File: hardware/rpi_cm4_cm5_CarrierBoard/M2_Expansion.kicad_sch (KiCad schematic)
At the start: 20 parts, among them J23 MDT420M03001, U38 ASAK-32.768KHZ-LRS-T

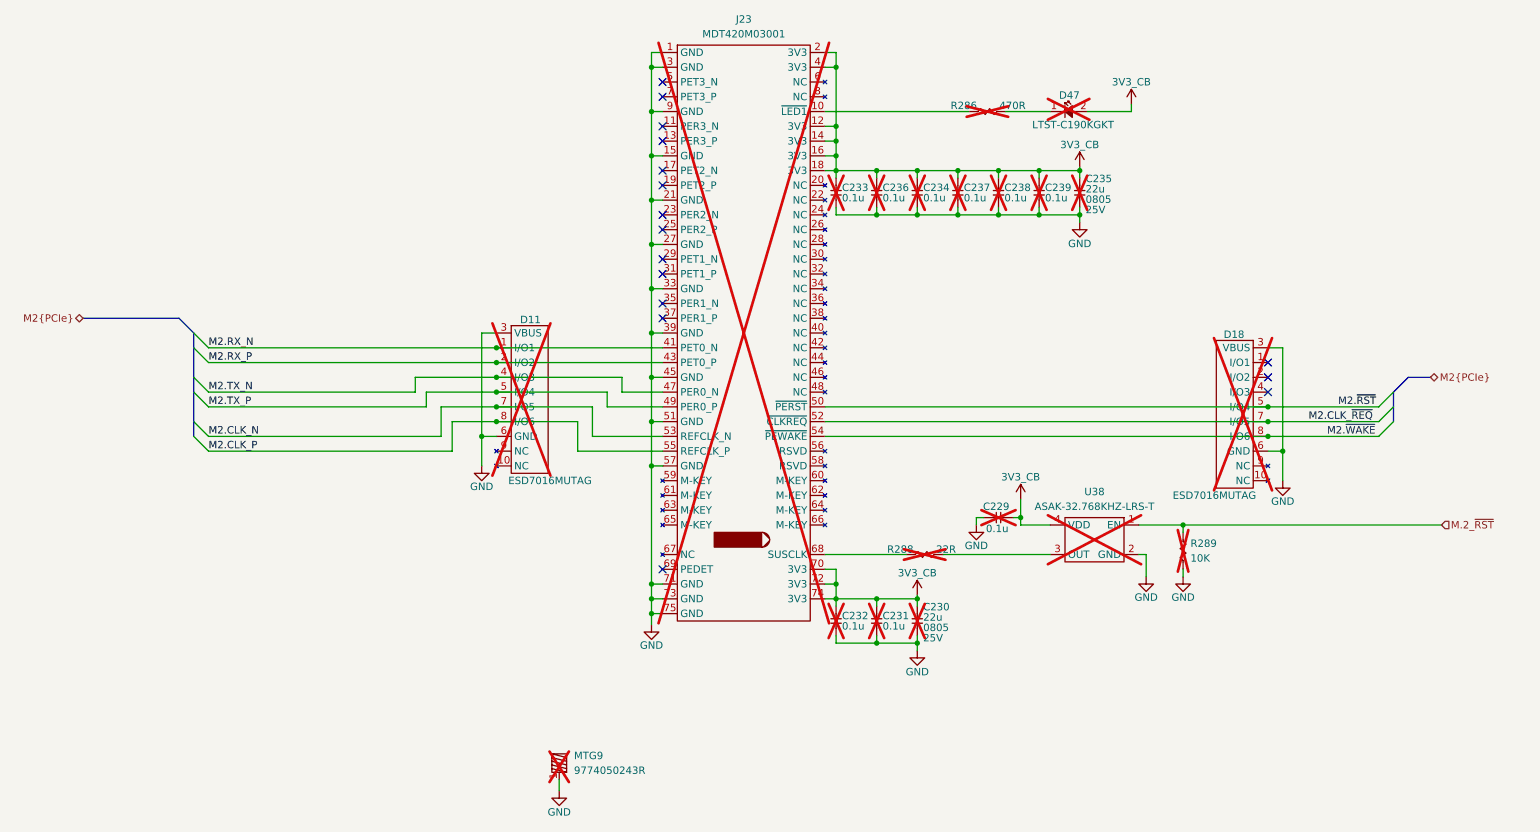
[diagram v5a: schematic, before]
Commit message: Document stackup Few changes to schematic based on preliminary PCB placement Update PinMux based on preliminary PCB placement and component positions
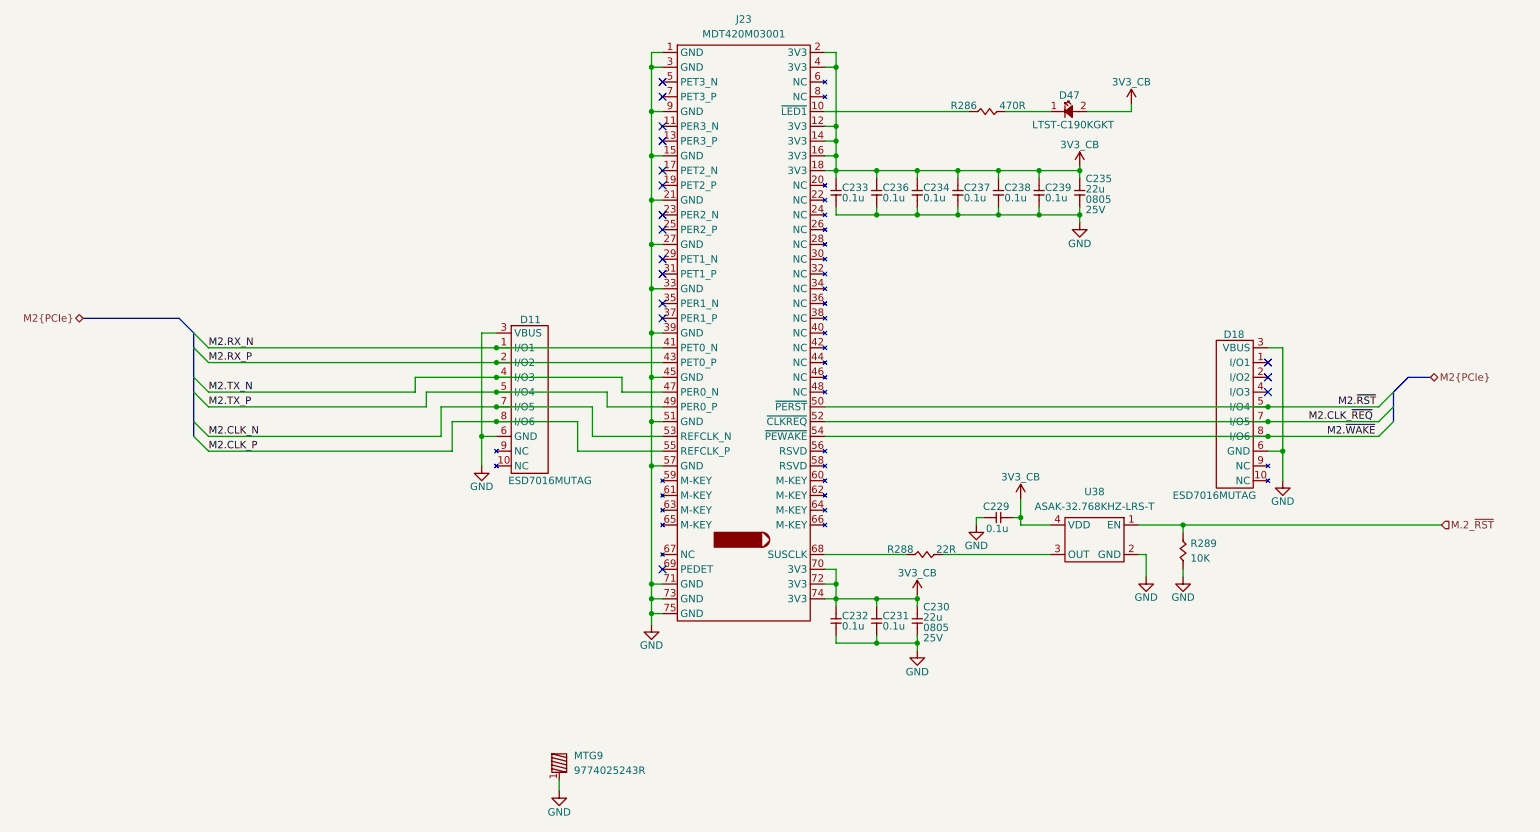
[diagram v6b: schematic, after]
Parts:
- removed MTG9: 9774050243R, footprint:9774050243R, symbol KicadCompDb:Miscellaneous/MISC_00008
- added MTG9: 9774025243R, footprint:9774025243R, symbol KicadCompDb:Miscellaneous/MISC_00009
- C229, C230, C231, C232, C233, C234, C235, C236, C237, C238, C239, D11, D18, D47, J23, R286, R288, R289, U38: now fitted
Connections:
- net GND: now also MTG9.1
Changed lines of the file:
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@@
 	(title_block
 		(title "RPI CMx Carrier")
-		(date "2025-12-07")
+		(date "2026-01-22")
 		(rev "2.00-0A")
 		(comment 1 "Jean-Francois Bilodeau")
@@
 		(in_bom yes)
 		(on_board yes)
-		(dnp yes)
+		(dnp no)
 		(property "Reference" "C231"
 			(at 167.386 145.796 90)
@@
 		(in_bom yes)
 		(on_board yes)
-		(dnp yes)
+		(dnp no)
 		(property "Reference" "D11"
 			(at 105.029 94.869 0)
@@
 		(in_bom yes)
 		(on_board yes)
-		(dnp yes)
+		(dnp no)
 		(property "Reference" "D18"
 			(at 229.616 97.409 0)
@@
 		(in_bom yes)
 		(on_board yes)
-		(dnp yes)
+		(dnp no)
 		(property "Reference" "C233"
 			(at 160.401 72.136 90)
@@
 		(in_bom yes)
 		(on_board yes)
-		(dnp yes)
+		(dnp no)
 		(property "Reference" "C229"
 			(at 184.658 127 0)
@@
 		(in_bom yes)
 		(on_board yes)
-		(dnp yes)
+		(dnp no)
 		(property "Reference" "R286"
 			(at 181.356 58.039 0)
@@
 		(in_bom yes)
 		(on_board yes)
-		(dnp yes)
+		(dnp no)
 		(property "Reference" "C232"
 			(at 160.401 145.796 90)
@@
 		(in_bom yes)
 		(on_board yes)
-		(dnp yes)
+		(dnp no)
 		(property "Reference" "C234"
 			(at 174.371 72.136 90)
@@
 		(in_bom yes)
 		(on_board yes)
-		(dnp yes)
+		(dnp no)
 		(property "Reference" "C235"
 			(at 202.311 70.612 90)
@@
 		(in_bom yes)
 		(on_board yes)
-		(dnp yes)
+		(dnp no)
 		(property "Reference" "C237"
 			(at 181.356 72.136 90)
@@
 		(in_bom yes)
 		(on_board yes)
-		(dnp yes)
+		(dnp no)
 		(property "Reference" "C236"
 			(at 167.386 72.136 90)
@@
 		(in_bom yes)
 		(on_board yes)
-		(dnp yes)
+		(dnp no)
 		(property "Reference" "C238"
 			(at 188.341 72.136 90)
@@
 	)
 	(symbol
+		(lib_id "KicadCompDb:Miscellaneous/MISC_00009")
+		(at 110.49 169.545 0)
+		(unit 1)
+		(exclude_from_sim no)
+		(in_bom yes)
+		(on_board yes)
+		(dnp no)
+		(fields_autoplaced yes)
+		(property "Reference" "MTG9"
+			(at 114.3 169.8624 0)
+			(effects
+				(font
+					(size 1.27 1.27)
+				)
+				(justify left)
+			)
+		)
+		(property "Value" "9774025243R"
+			(at 114.3 172.4024 0)
+			(effects
+				(font
+					(size 1.27 1.27)
+				)
+				(justify left)
+			)
+		)
+		(property "Footprint" "footprint:9774025243R"
+			(at 110.49 169.545 0)
+			(effects
+				(font
+					(size 1.27 1.27)
+				)
+				(hide yes)
+			)
+		)
+		(property "Datasheet" "https://www.we-online.com/components/products/datasheet/9774025243R.pdf"
+			(at 110.49 169.545 0)
+			(effects
+				(font
+					(size 1.27 1.27)
+				)
+				(hide yes)
+			)
+		)
+		(property "Description" "RND STANDOFF M2X0.4 STEEL 2.50MM"
+			(at 110.49 169.545 0)
+			(effects
+				(font
+					(size 1.27 1.27)
+				)
+				(hide yes)
+			)
+		)
+		(property "Type" "RND STANDOFF M2X0.4 STEEL 2.50MM"
+			(at 110.49 169.545 0)
+			(show_name yes)
+			(effects
+				(font
+					(size 1.27 1.27)
+				)
+				(hide yes)
+			)
+		)
+		(property "Package" "M2x0.4"
+			(at 110.49 169.545 0)
+			(show_name yes)
+			(effects
+				(font
+					(size 1.27 1.27)
+				)
+				(hide yes)
+			)
+		)
+		(property "Operating Temperature" "-40°C ~ 150°C"
+			(at 110.49 169.545 0)
+			(show_name yes)
+			(effects
+				(font
+					(size 1.27 1.27)
+				)
+				(hide yes)
+			)
+		)
+		(property "Dimensions" "4.35mm x 3.91mm"
+			(at 110.49 169.545 0)
+			(show_name yes)
+			(effects
+				(font
+					(size 1.27 1.27)
+				)
+				(hide yes)
+			)
+		)
+		(property "Manufacturer" "Würth Elektronik"
+			(at 110.49 169.545 0)
+			(show_name yes)
+			(effects
+				(font
+					(size 1.27 1.27)
+				)
+				(hide yes)
+			)
+		)
+		(property "Manufacturer Part Number" "9774025243R"
+			(at 110.49 169.545 0)
+			(show_name yes)
+			(effects
+				(font
+					(size 1.27 1.27)
+				)
+				(hide yes)
+			)
+		)
+		(property "Distributor" "DigiKey"
+			(at 110.49 169.545 0)
+			(show_name yes)
+			(effects
+				(font
+					(size 1.27 1.27)
+				)
+				(hide yes)
+			)
+		)
+		(property "Distributor Part Number" "732-7079-1-ND"
+			(at 110.49 169.545 0)
+			(show_name yes)
+			(effects
+				(font
+					(size 1.27 1.27)
+				)
+				(hide yes)
+			)
+		)
+		(pin "1"
+		)
+		(instances
+			(project ""
+				(path "/7dcdf741-90ca-4333-848c-806f4d64158e/9de20a6e-0c13-4cd2-9bfa-6170acf466d0"
+					(reference "MTG9")
+					(unit 1)
+				)
+			)
+		)
+	)
+	(symbol
 		(lib_id "KiCad_Pwr_Symbols:GND")
 		(at 219.075 139.065 0)
@@
 		(in_bom yes)
 		(on_board yes)
-		(dnp yes)
+		(dnp no)
 		(property "Reference" "R289"
 			(at 220.345 133.3499 90)
@@
 		(in_bom yes)
 		(on_board yes)
-		(dnp yes)
+		(dnp no)
 		(fields_autoplaced yes)
 		(property "Reference" "J23"
@@
 		(in_bom yes)
 		(on_board yes)
-		(dnp yes)
+		(dnp no)
 		(property "Reference" "R288"
 			(at 170.434 134.366 0)
@@
 		(in_bom yes)
 		(on_board yes)
-		(dnp yes)
+		(dnp no)
 		(property "Reference" "U38"
 			(at 203.835 124.46 0)
@@
 	)
 	(symbol
-		(lib_id "KicadCompDb:Miscellaneous/MISC_00008")
-		(at 110.49 169.545 0)
-		(unit 1)
-		(exclude_from_sim no)
-		(in_bom yes)
-		(on_board yes)
-		(dnp yes)
-		(fields_autoplaced yes)
-		(property "Reference" "MTG9"
-			(at 114.3 169.8624 0)
-			(effects
-				(font
-					(size 1.27 1.27)
-				)
-				(justify left)
-			)
-		)
-		(property "Value" "9774050243R"
-			(at 114.3 172.4024 0)
-			(effects
-				(font
-					(size 1.27 1.27)
-				)
-				(justify left)
-			)
-		)
-		(property "Footprint" "footprint:9774050243R"
-			(at 110.49 169.545 0)
-			(effects
-				(font
-					(size 1.27 1.27)
-				)
-				(hide yes)
-			)
-		)
-		(property "Datasheet" ""
-			(at 110.49 169.545 0)
-			(effects
-				(font
-					(size 1.27 1.27)
-				)
-				(hide yes)
-			)
-		)
-		(property "Description" "ROUND STANDOFF M2X0.4 STEEL 5MM"
-			(at 110.49 169.545 0)
-			(effects
-				(font
-					(size 1.27 1.27)
-				)
-				(hide yes)
-			)
-		)
-		(property "Type" "ROUND STANDOFF M2X0.4 STEEL 5MM"
-			(at 110.49 169.545 0)
-			(show_name yes)
-			(effects
-				(font
-					(size 1.27 1.27)
-				)
-				(hide yes)
-			)
-		)
-		(property "Package" "M2x0.4"
-			(at 110.49 169.545 0)
-			(show_name yes)
-			(effects
-				(font
-					(size 1.27 1.27)
-				)
-				(hide yes)
-			)
-		)
-		(property "Operating Temperature" "-40°C ~ 150°C"
-			(at 110.49 169.545 0)
-			(show_name yes)
-			(effects
-				(font
-					(size 1.27 1.27)
-				)
-				(hide yes)
-			)
-		)
-		(property "Dimensions" "4.35mm x 6.40mm"
-			(at 110.49 169.545 0)
-			(show_name yes)
-			(effects
-				(font
-					(size 1.27 1.27)
-				)
-				(hide yes)
-			)
-		)
-		(property "Manufacturer" "Würth Elektronik"
-			(at 110.49 169.545 0)
-			(show_name yes)
-			(effects
-				(font
-					(size 1.27 1.27)
-				)
-				(hide yes)
-			)
-		)
-		(property "Manufacturer Part Number" "9774050243R"
-			(at 110.49 169.545 0)
-			(show_name yes)
-			(effects
-				(font
-					(size 1.27 1.27)
-				)
-				(hide yes)
-			)
-		)
-		(property "Distributor" "DigiKey"
-			(at 110.49 169.545 0)
-			(show_name yes)
-			(effects
-				(font
-					(size 1.27 1.27)
-				)
-				(hide yes)
-			)
-		)
-		(property "Distributor Part Number" "732-7097-1-ND"
-			(at 110.49 169.545 0)
-			(show_name yes)
-			(effects
-				(font
-					(size 1.27 1.27)
-				)
-				(hide yes)
-			)
-		)
-		(pin "1"
-		)
-		(instances
-			(project ""
-				(path "/7dcdf741-90ca-4333-848c-806f4d64158e/9de20a6e-0c13-4cd2-9bfa-6170acf466d0"
-					(reference "MTG9")
-					(unit 1)
-				)
-			)
-		)
-	)
-	(symbol
 		(lib_id "KicadCompDb:Capacitors/CAP_CER_SMT_00011")
 		(at 173.355 149.225 90)
@@
 		(in_bom yes)
 		(on_board yes)
-		(dnp yes)
+		(dnp no)
 		(property "Reference" "C230"
 			(at 174.371 144.272 90)
@@
 		(in_bom yes)
 		(on_board yes)
-		(dnp yes)
+		(dnp no)
 		(property "Reference" "D47"
 			(at 199.517 56.261 0)
@@
 		(in_bom yes)
 		(on_board yes)
-		(dnp yes)
+		(dnp no)
 		(property "Reference" "C239"
 			(at 195.326 72.136 90)

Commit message: Adjust length matching (transmitter vx receiver matching)
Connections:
- net M2.CLK_~{REQ} renamed M2.~{REQ}
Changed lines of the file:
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@@
 		)
 	)
-	(label "M2.CLK_~{REQ}"
-		(at 240.665 112.395 0)
+	(label "M2.~{REQ}"
+		(at 245.745 112.395 0)
 		(effects
 			(font

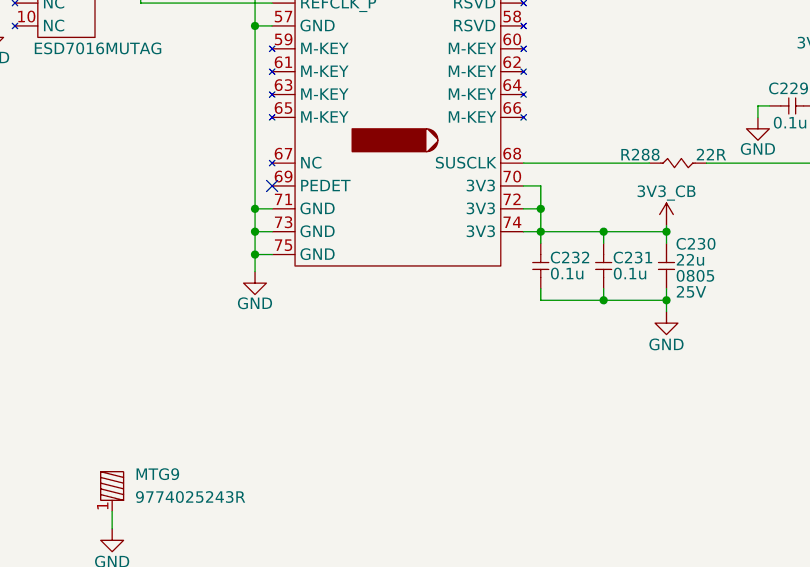
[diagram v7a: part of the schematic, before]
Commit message: Significant update Stackup changed from 6 to 8 layers Changed design notes accordingly Re-routed all differential pairs and length match / skew match Fanout critical signals away from dense areas 95% routing completed
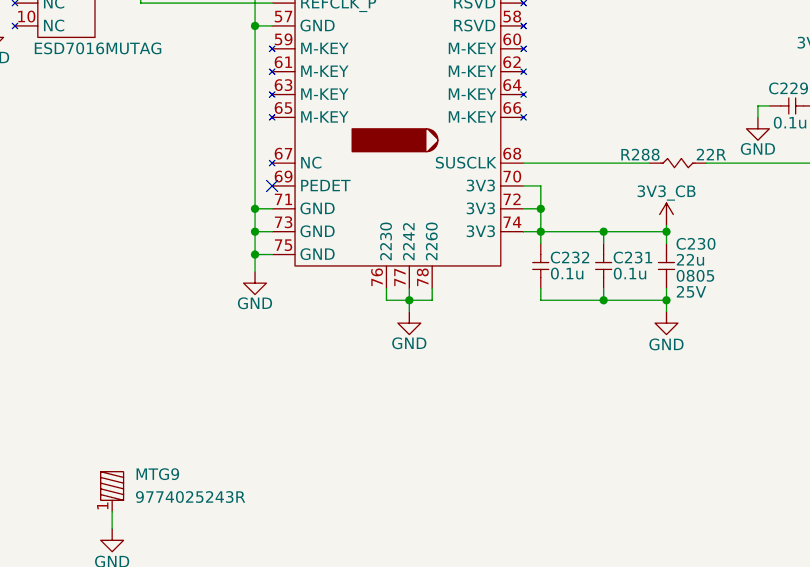
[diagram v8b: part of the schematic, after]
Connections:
- net GND: now also J23.76 (2230), J23.77 (2242), J23.78 (2260)
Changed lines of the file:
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@@
 	(title_block
 		(title "RPI CMx Carrier")
-		(date "2026-01-22")
+		(date "2026-02-13")
 		(rev "2.00-0A")
 		(comment 1 "Jean-Francois Bilodeau")
@@
 	)
 	(junction
+		(at 144.78 150.495)
+		(diameter 0)
+		(color 0 0 0 0)
+	)
+	(junction
 		(at 159.385 61.595)
 		(diameter 0)
@@
 	(wire
 		(pts
+			(xy 144.78 150.495) (xy 144.78 151.765)
+		)
+		(stroke
+			(width 0)
+			(type default)
+		)
+	)
+	(wire
+		(pts
 			(xy 201.295 75.565) (xy 201.295 76.835)
 		)
@@
 	(wire
 		(pts
+			(xy 142.24 150.495) (xy 144.78 150.495)
+		)
+		(stroke
+			(width 0)
+			(type default)
+		)
+	)
+	(wire
+		(pts
 			(xy 127.635 112.395) (xy 129.54 112.395)
 		)
@@
 	(wire
 		(pts
+			(xy 142.24 149.225) (xy 142.24 150.495)
+		)
+		(stroke
+			(width 0)
+			(type default)
+		)
+	)
+	(wire
+		(pts
 			(xy 127.635 89.535) (xy 129.54 89.535)
 		)
@@
 	(wire
 		(pts
+			(xy 147.32 149.225) (xy 147.32 150.495)
+		)
+		(stroke
+			(width 0)
+			(type default)
+		)
+	)
+	(wire
+		(pts
 			(xy 166.37 142.875) (xy 173.355 142.875)
 		)
@@
 	(wire
 		(pts
+			(xy 144.78 150.495) (xy 147.32 150.495)
+		)
+		(stroke
+			(width 0)
+			(type default)
+		)
+	)
+	(wire
+		(pts
 			(xy 166.37 69.215) (xy 166.37 70.485)
 		)
@@
 	(wire
 		(pts
+			(xy 144.78 149.225) (xy 144.78 150.495)
+		)
+		(stroke
+			(width 0)
+			(type default)
+		)
+	)
+	(wire
+		(pts
 			(xy 201.295 76.835) (xy 194.31 76.835)
 		)
@@
 		(pin "0"
 		)
+		(pin "77"
+		)
+		(pin "78"
+		)
+		(pin "76"
+		)
 		(instances
 			(project ""
@@
 					(unit 1)
 				)
+			)
+		)
+	)
+	(symbol
+		(lib_id "KiCad_Pwr_Symbols:GND")
+		(at 144.78 151.765 0)
+		(unit 1)
+		(exclude_from_sim no)
+		(in_bom yes)
+		(on_board yes)
+		(dnp no)
+		(property "Reference" "#PWR02"
+			(at 144.78 158.115 0)
+			(effects
+				(font
+					(size 1.27 1.27)
+				)
+				(hide yes)
+			)
+		)
+		(property "Value" "GND"
+			(at 144.78 155.321 0)
+			(effects
+				(font
+					(size 1.27 1.27)
+				)
+			)
+		)
+		(property "Footprint" ""
+			(at 144.78 151.765 0)
+			(effects
+				(font
+					(size 1.27 1.27)
+				)
+				(hide yes)
+			)
+		)
+		(property "Datasheet" ""
+			(at 144.78 151.765 0)
+			(effects
+				(font
+					(size 1.27 1.27)
+				)
+				(hide yes)
+			)
+		)
+		(property "Description" "Power symbol creates a global label with name \"GND\" , ground"
+			(at 144.78 151.765 0)
+			(effects
+				(font
+					(size 1.27 1.27)
+				)
+				(hide yes)
+			)
+		)
+		(pin "1"
+		)
+		(instances
+			(project "rpi_cm4_cm5_CarrierBoard"
+				(path "/7dcdf741-90ca-4333-848c-806f4d64158e/9de20a6e-0c13-4cd2-9bfa-6170acf466d0"
+					(reference "#PWR02")
+					(unit 1)
+				)
